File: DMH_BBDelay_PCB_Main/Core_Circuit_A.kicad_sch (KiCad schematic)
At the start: 98 parts, among them J22 Conn_01x04, J23 Conn_01x04, J24 Conn_01x04, J25 Conn_01x04, J26 Conn_01x08, J27 Conn_01x08, J28 Conn_01x08, J29 Conn_01x08, J34 Conn_01x04, J35 Conn_01x02, J38 Conn_01x08, J39 Conn_01x04, Q19 BC548, Q3 J113, SW3 SW_SPDT, U1 TL074, U2 TL074, U22 V3205, U24 V3205, U25 V3205, U3 V3205, U4 CD4046, U9 40106

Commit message: Added notes for adjustment to be made
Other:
- note added: "Adjust these to account for the multiple V3205 in series"
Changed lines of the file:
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@@
+	)
+	(rectangle
+		(start 119.38 179.07)
+		(end 142.24 187.96)
+		(stroke
+			(width 0)
+			(type default)
+		)
+		(fill
+			(type none)
+		)
 	)
 	(rectangle
@@
 		)
 	)
+	(text "Adjust these to account for the multiple V3205 in series"
+		(exclude_from_sim no)
+		(at 165.1 194.31 0)
+		(effects
+			(font
+				(size 1.27 1.27)
+			)
+		)
+	)
+	(text_box "Idea in case phaser mode doesn't sound good due to the 5kHz filtering:\n\nUse extra CD4053 per channel to bypass the Input and Output filters.\nThe 3rd switch in the CD4053 can be used to add a resistor to -12V to add the 2.5V offset needed for the V3205.\nCommand the CD4053 with a 3-way DPDT, combining the range cap selection."
+		(exclude_from_sim no)
+		(at 12.7 114.3 0)
+		(size 52.07 25.4)
+		(margins 0.9525 0.9525 0.9525 0.9525)
+		(stroke
+			(width 0)
+			(type solid)
+		)
+		(fill
+			(type none)
+		)
+		(effects
+			(font
+				(size 1.27 1.27)
+			)
+			(justify left top)
+		)
+	)

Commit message: Added extra V3205 to channel B
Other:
- note added: "Bring back to 6k2 to avoid clock noise without filter"
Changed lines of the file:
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@@
 		)
 	)
+	(circle
+		(center 233.68 125.73)
+		(radius 5.08)
+		(stroke
+			(width 0)
+			(type default)
+		)
+		(fill
+			(type none)
+		)
+	)
 	(text "V3205 decoupling caps"
 		(exclude_from_sim no)
@@
 		)
 	)
+	(text "Bring back to 6k2 to avoid\nclock noise without filter"
+		(exclude_from_sim no)
+		(at 252.73 133.35 0)
+		(effects
+			(font
+				(size 1.27 1.27)
+			)
+		)
+	)
 	(text "Adjust these to account for the multiple V3205 in series"
 		(exclude_from_sim no)
@@
 	)
 	(global_label "VGG_m"
-		(shape output)
+		(shape input)
 		(at 114.3 109.22 180)
 		(fields_autoplaced yes)
@@
 	)
 	(global_label "VGG_m"
-		(shape output)
+		(shape input)
 		(at 171.45 66.04 180)
 		(fields_autoplaced yes)

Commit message: Set S&H pulse resistor back to 6k2
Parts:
- R35: value 10k -> 6k2
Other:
- note removed: "Bring back to 6k2 to avoid clock noise without filter"
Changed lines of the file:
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@@
 		)
 	)
-	(circle
-		(center 233.68 125.73)
-		(radius 5.08)
-		(stroke
-			(width 0)
-			(type default)
-		)
-		(fill
-			(type none)
-		)
-	)
 	(text "V3205 decoupling caps"
 		(exclude_from_sim no)
@@
 		)
 	)
-	(text "Bring back to 6k2 to avoid\nclock noise without filter"
-		(exclude_from_sim no)
-		(at 252.73 133.35 0)
-		(effects
-			(font
-				(size 1.27 1.27)
-			)
-		)
-	)
 	(text "Adjust these to account for the multiple V3205 in series"
 		(exclude_from_sim no)
@@
 			)
 		)
-		(property "Value" "10k"
+		(property "Value" "6k2"
 			(at 233.68 126.9999 0)
 			(show_name no)

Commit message: Validating quad V3205 on breadboard in progress
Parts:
- removed C65: 1nF, Capacitor_THT:C_Disc_D3.0mm_W2.0mm_P2.50mm, symbol Device:C
- removed R186: 100R, Resistor_THT:R_Axial_DIN0207_L6.3mm_D2.5mm_P7.62mm_Horizontal, symbol Device:R_US
- added C92: 220pF, Capacitor_THT:C_Disc_D3.0mm_W2.0mm_P2.50mm, symbol Device:C
- R200: value 100k -> 47k
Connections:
- net -12V: now also R32.1
- net GND: now also C92.1; no longer R32.1
- net Input Filter A/Out: now also U3.7 (In)
- net at C13.1, R32.2, U25.4 (Out2): now also C92.2

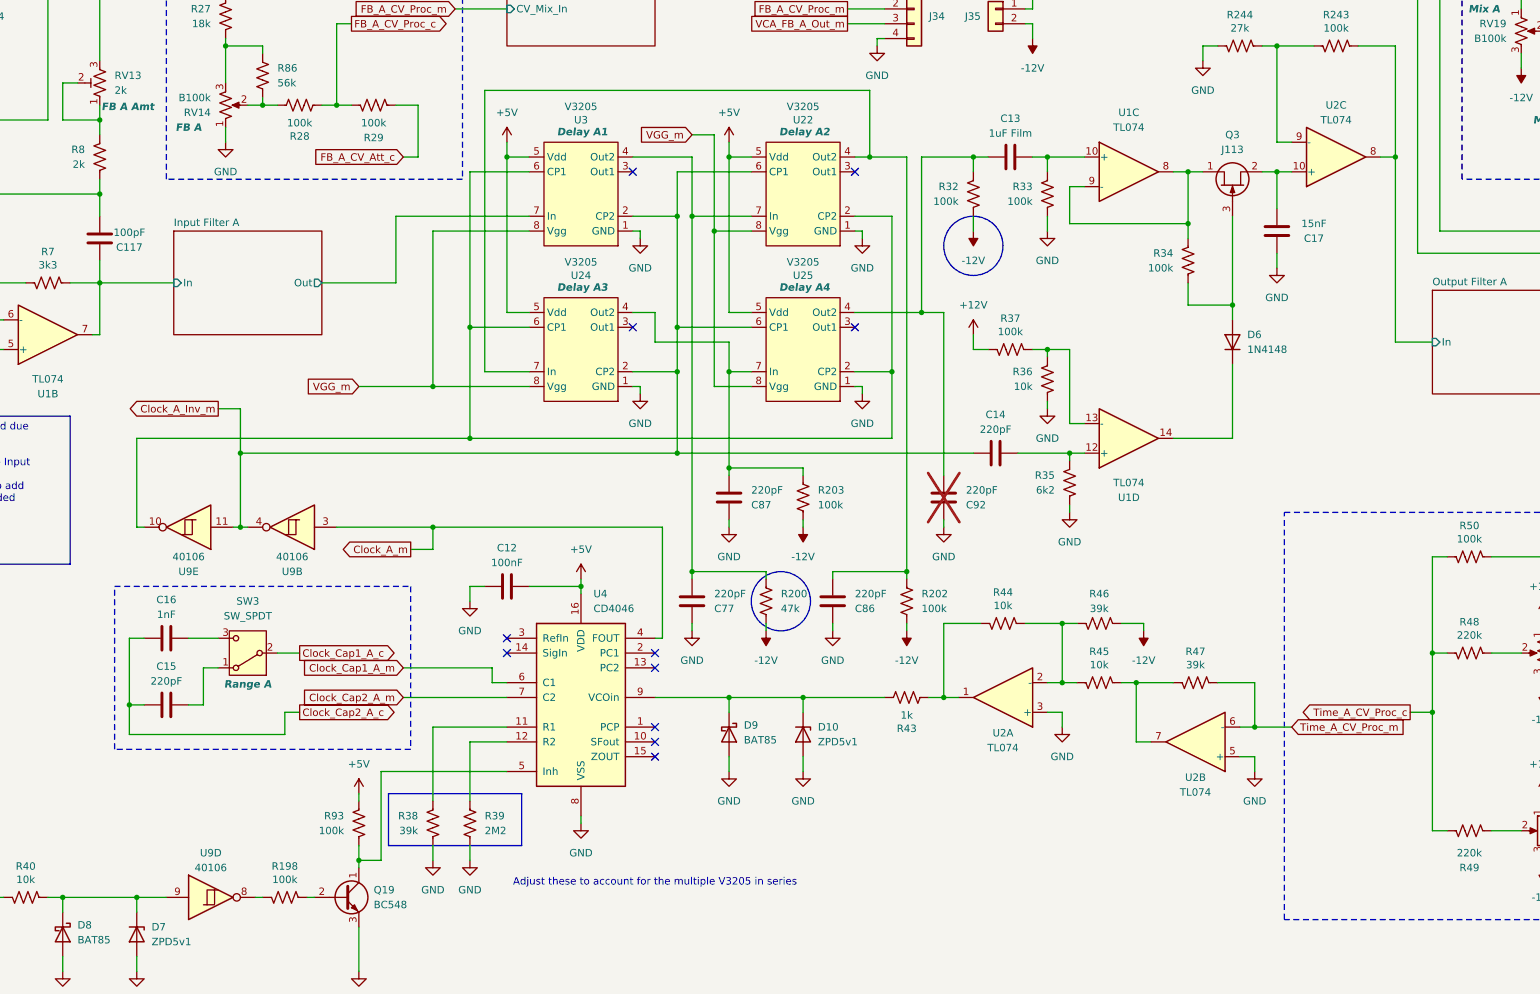
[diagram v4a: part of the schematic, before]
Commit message: Added extra hex inverters to buffer clocks
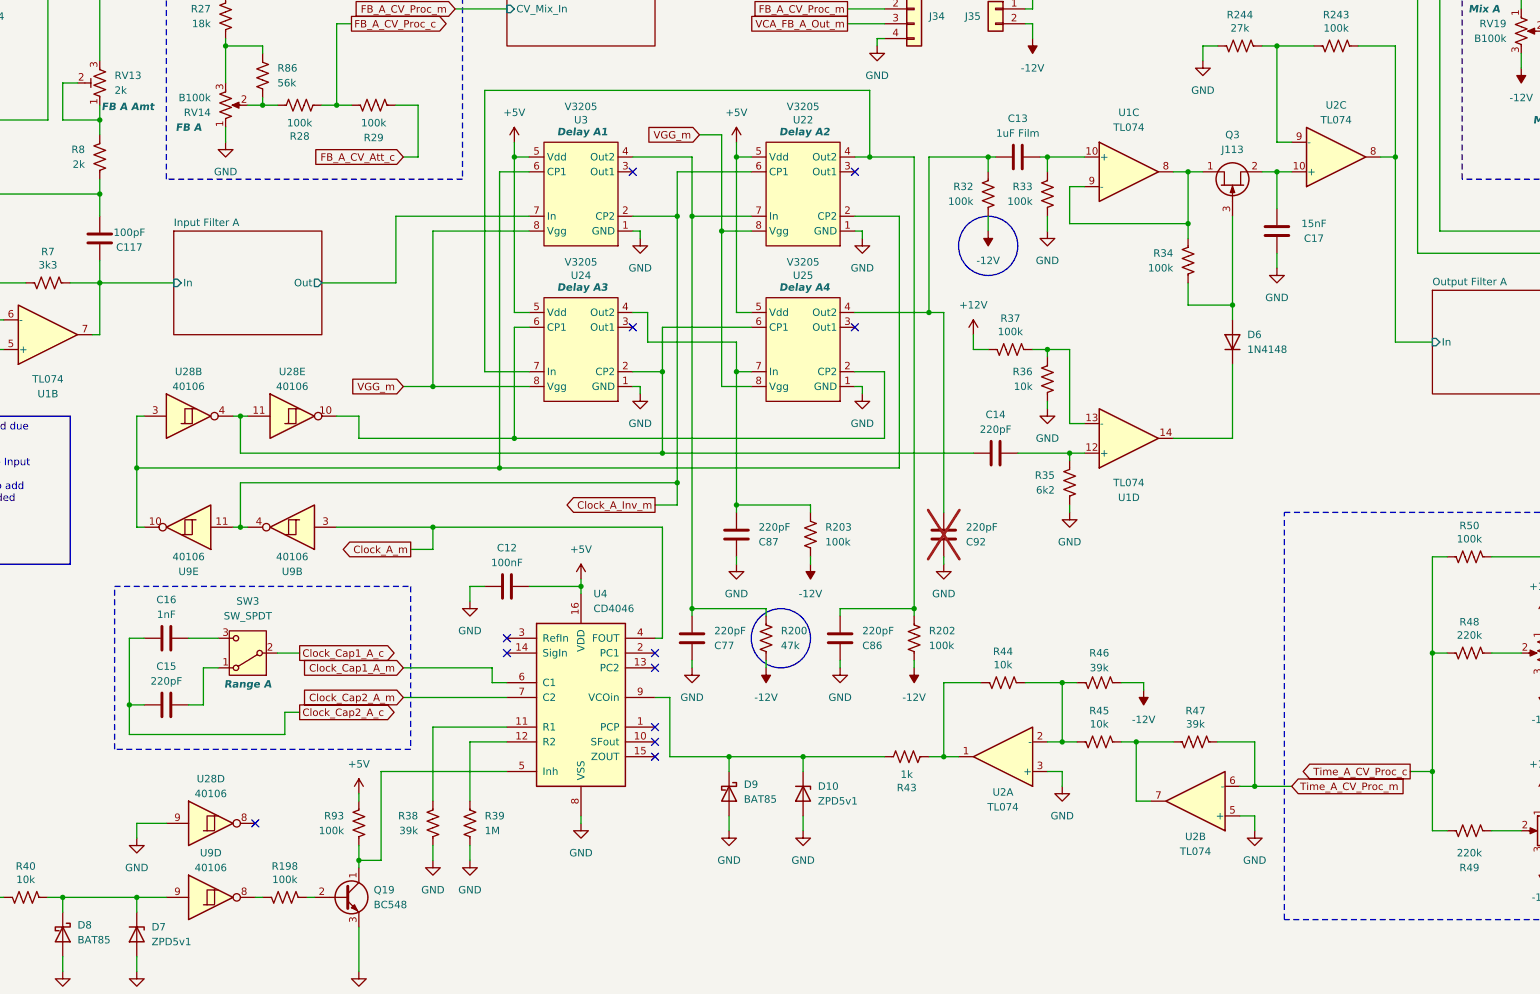
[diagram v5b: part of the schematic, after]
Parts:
- added U28: 40106, Package_DIP:DIP-14_W7.62mm_Socket, symbol 4xxx:40106
- R39: value 2M2 -> 1M
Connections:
- net Clock_A_Inv_m: no longer C14.1, U24.2 (CP2), U25.6 (CP1)
- net GND: now also U28.9
- net at U22.2 (CP2), U3.6 (CP1), U9.10: now also U28.3; no longer U24.6 (CP1), U25.2 (CP2)
- new net: U24.6 (CP1), U25.2 (CP2), U28.10
- new net: C14.1, U24.2 (CP2), U25.6 (CP1), U28.11, U28.4
- no-connect marks 15 -> 16
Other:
- note removed: "Adjust these to account for the multiple V3205 in series"
- moved on the sheet: C13, C77, C86, C87, C92, D10, D9, R200, R202, R203, R32, R43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

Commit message: Breadboarding continues
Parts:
- C77, C86: value 220pF -> 100pF
- C87: value 220pF -> 470pF
- R200: value 47k -> 10k
- R202, R203, R32: value 100k -> 10k
- renumbered U28 to U9
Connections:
- net -12V: no longer R200.1, R202.1, R203.1, R32.1
- net GND: now also R200.1, R202.1, R203.1, R32.1
- net at U24.6 (CP1), U25.2 (CP2): now also U9.12; no longer U9.10
- net at C14.1, U24.2 (CP2), U25.6 (CP1): now also U9.13, U9.2; no longer U9.11, U9.4
- net at U22.2 (CP2), U3.6 (CP1), U9.10: now also U9.1; no longer U9.3
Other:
- moved on the sheet: C15, C16, SW3

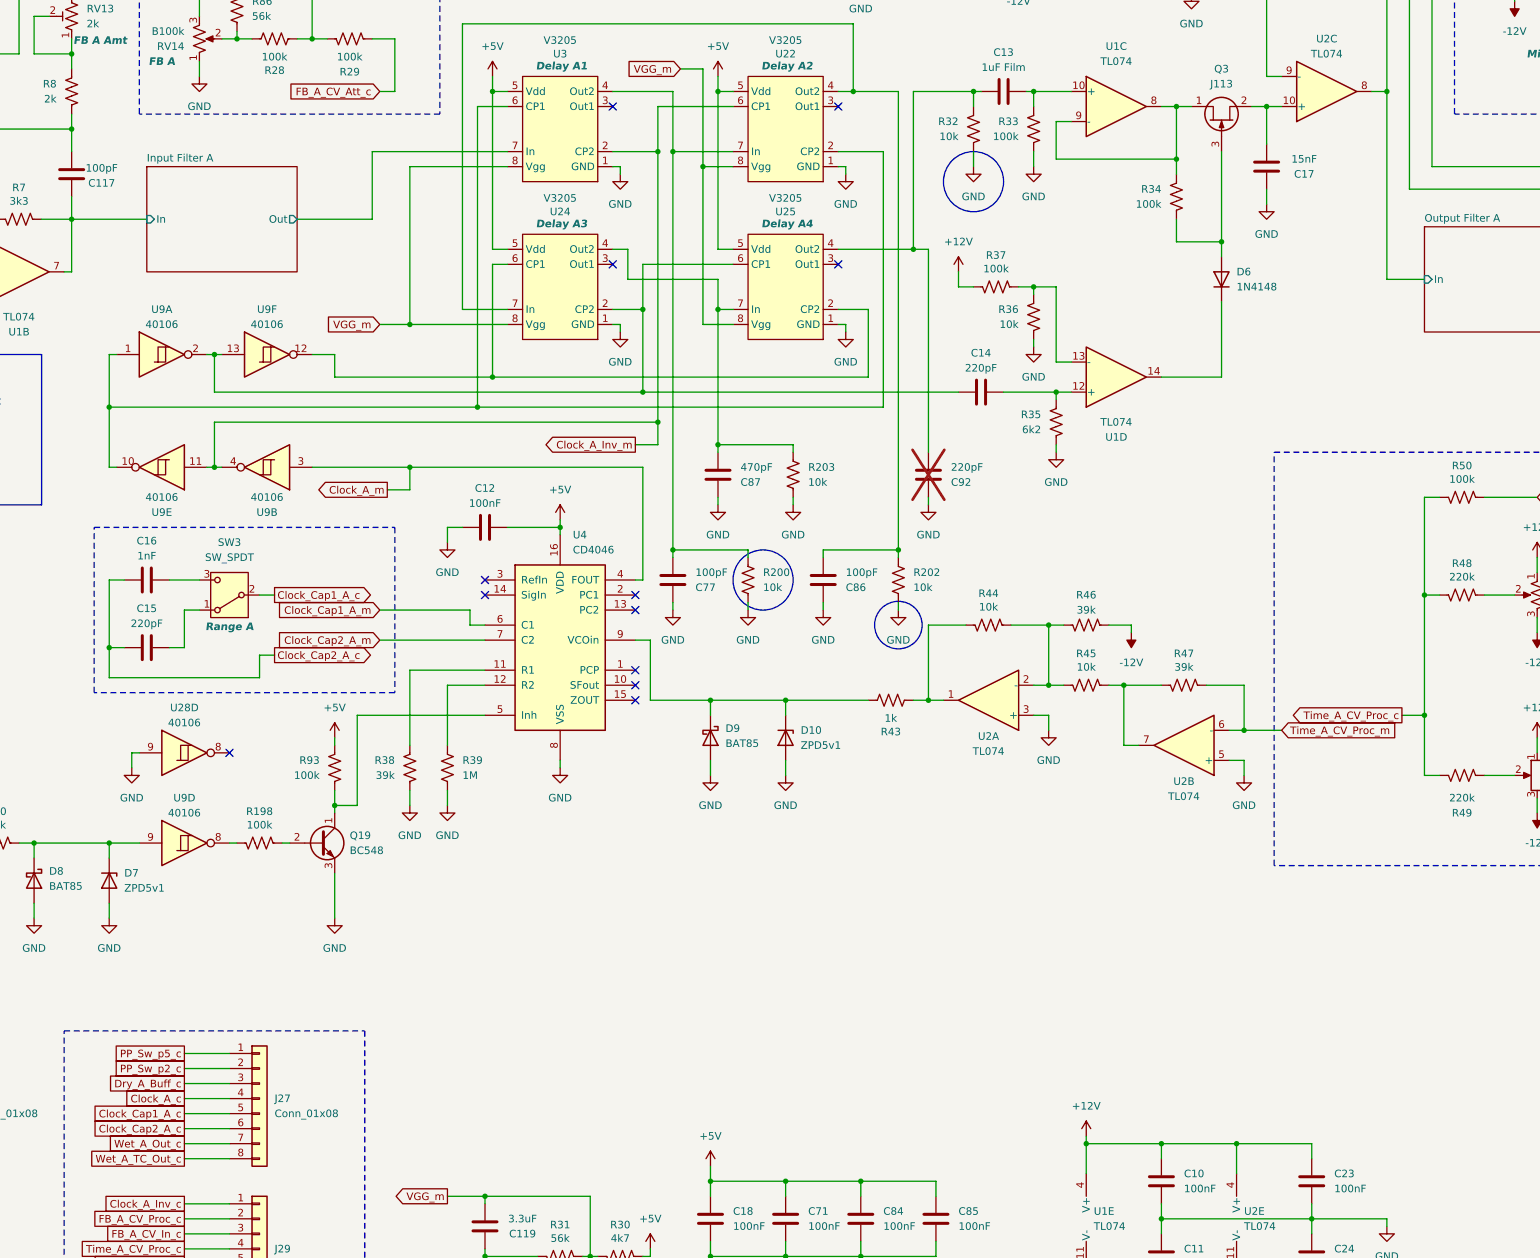
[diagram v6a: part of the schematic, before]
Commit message: clock buffer with opamp
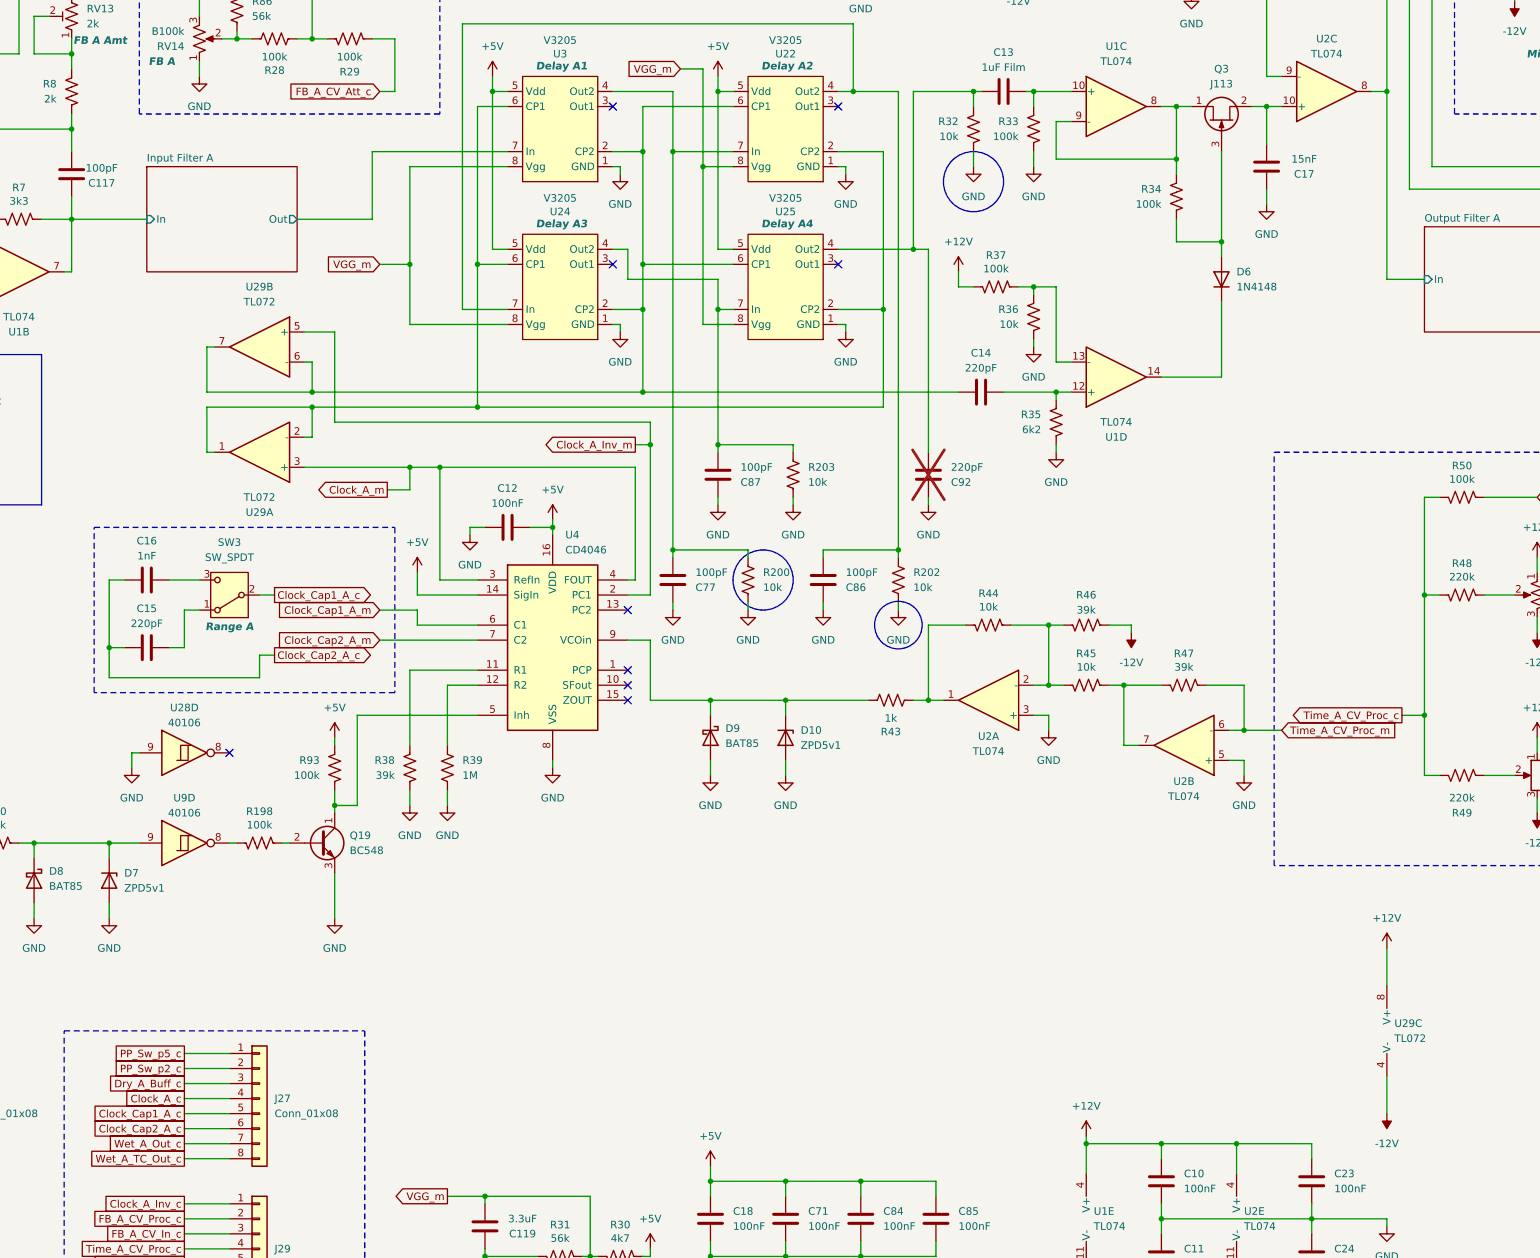
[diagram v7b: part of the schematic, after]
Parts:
- removed unit 2 of U9
- removed unit 6 of U9
- removed unit 5 of U9
- removed unit 1 of U9
- added U29: TL072, Package_DIP:DIP-8_W7.62mm_Socket, symbol Amplifier_Operational:TL072
- C87: value 470pF -> 100pF
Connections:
- net +12V: now also U29.8 (V+)
- net +5V: now also U4.14 (SigIn)
- net -12V: now also U29.4 (V-)
- net Clock_A_Inv_m: now also U4.2 (PC1), U29.5 (+); no longer U22.6 (CP1), U3.2 (CP2)
- net Clock_A_m: now also U4.3 (RefIn), U29.3 (+)
- net at U24.6 (CP1), U25.2 (CP2): now also U22.2 (CP2), U3.6 (CP1), U29.1, U29.2 (-)
- net at C14.1, U24.2 (CP2), U25.6 (CP1): now also U22.6 (CP1), U3.2 (CP2), U29.6 (-), U29.7
- no-connect marks 16 -> 13
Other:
- moved on the sheet: C12, U4
